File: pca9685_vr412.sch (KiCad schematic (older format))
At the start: 51 parts, among them J1 I2Cbus, J10 C4GND, J11 C4VDD, J12 C4VDD, J13 C4VDD, J14 C4VDD, J15 USB_B_Micro, J16 Conn_02x20, J2 Conn_01x02, J3 LED03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

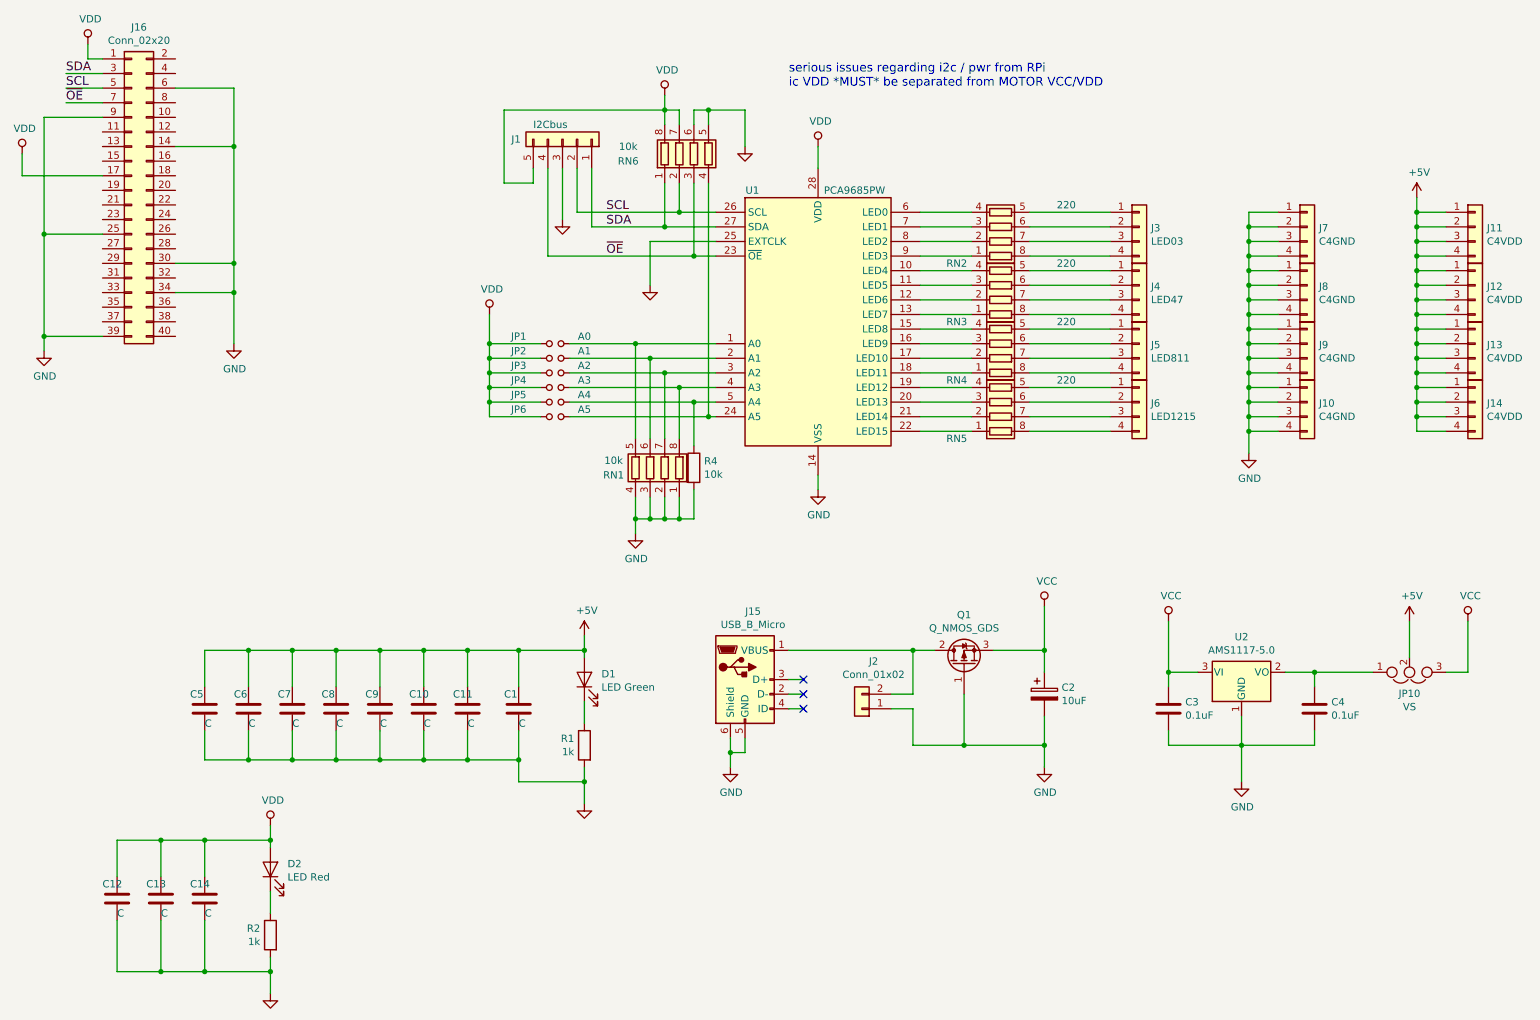
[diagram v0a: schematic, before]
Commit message: Updated layout
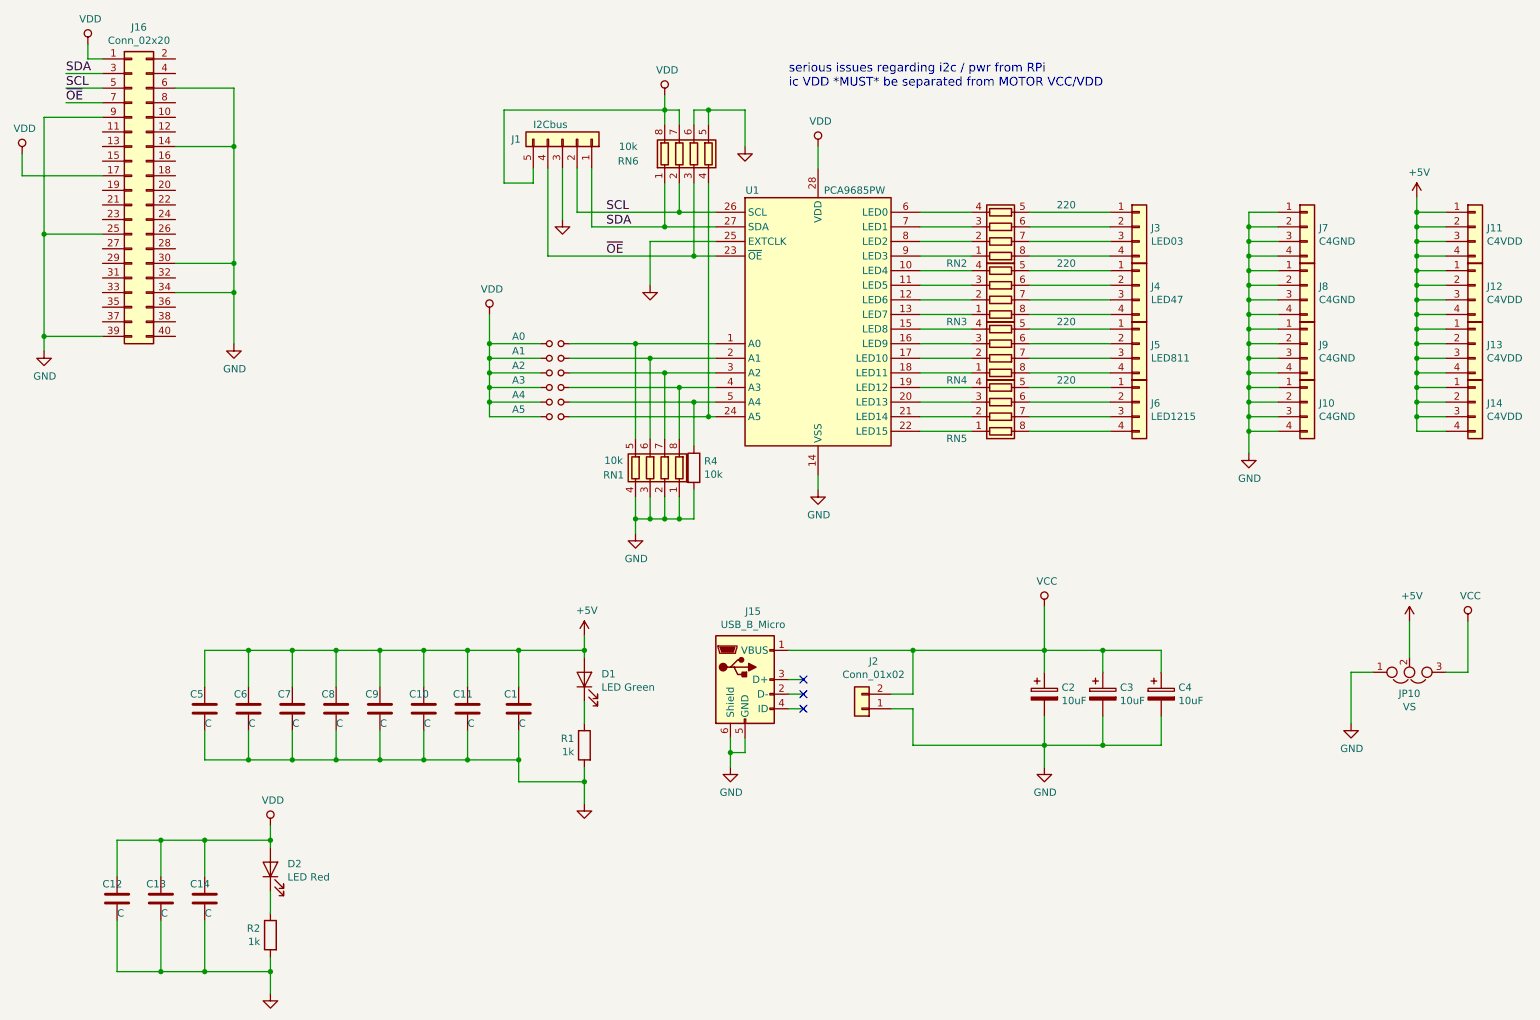
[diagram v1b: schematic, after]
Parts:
- removed C3, C4: 0.1uF, Capacitors_SMD:C_0603_HandSoldering, symbol C
- removed Q1: Q_NMOS_GDS, TO_SOT_Packages_SMD:SOT-23, symbol Q_PMOS_GDS
- removed U2: AMS1117-5.0, TO_SOT_Packages_SMD:SOT-223-3_TabPin2, symbol AMS1117-5.0
- added C3, C4: 10uF, Capacitors_SMD:CP_Elec_5x5.3, symbol CP
- renumbered JP1 to A0, JP2 to A1, JP3 to A2, JP4 to A3, JP5 to A4, JP6 to A5
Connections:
- net GND: now also JP10.1, C3.2, C4.2
- net VCC: now also J15.1 (VBUS), J2.2 (Pin_2), C3.1, C4.1
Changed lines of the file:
@@
 $EndComp
 $Comp
-L Jumper_NO_Small JP1
+L Jumper_NO_Small A0
 U 1 1 5D06A234
 P 4300 2950
-F 0 "JP1" H 4050 3000 50  0000 C CNN
-F 1 "A0" H 4500 3000 50  0000 C CNN
+F 0 "A0" H 4050 3000 50  0000 C CNN
+F 1 "A0" H 4500 3000 50  0001 C CNN
 F 2 "Jumper:SolderJumper_Triangular_0603" H 4300 2950 50  0001 C CNN
 F 3 "" H 4300 2950 50  0001 C CNN
@@
 $EndComp
 $Comp
-L Jumper_NO_Small JP2
+L Jumper_NO_Small A1
 U 1 1 5D06A4A7
 P 4300 3050
-F 0 "JP2" H 4050 3100 50  0000 C CNN
-F 1 "A1" H 4500 3100 50  0000 C CNN
+F 0 "A1" H 4050 3100 50  0000 C CNN
+F 1 "A1" H 4500 3100 50  0001 C CNN
 F 2 "Jumper:SolderJumper_Triangular_0603" H 4300 3050 50  0001 C CNN
 F 3 "" H 4300 3050 50  0001 C CNN
@@
 $EndComp
 $Comp
-L Jumper_NO_Small JP3
+L Jumper_NO_Small A2
 U 1 1 5D06A4FE
 P 4300 3150
-F 0 "JP3" H 4050 3200 50  0000 C CNN
-F 1 "A2" H 4500 3200 50  0000 C CNN
+F 0 "A2" H 4050 3200 50  0000 C CNN
+F 1 "A2" H 4500 3200 50  0001 C CNN
 F 2 "Jumper:SolderJumper_Triangular_0603" H 4300 3150 50  0001 C CNN
 F 3 "" H 4300 3150 50  0001 C CNN
@@
 $EndComp
 $Comp
-L Jumper_NO_Small JP4
+L Jumper_NO_Small A3
 U 1 1 5D06A550
 P 4300 3250
-F 0 "JP4" H 4050 3300 50  0000 C CNN
-F 1 "A3" H 4500 3300 50  0000 C CNN
+F 0 "A3" H 4050 3300 50  0000 C CNN
+F 1 "A3" H 4500 3300 50  0001 C CNN
 F 2 "Jumper:SolderJumper_Triangular_0603" H 4300 3250 50  0001 C CNN
 F 3 "" H 4300 3250 50  0001 C CNN
@@
 $EndComp
 $Comp
-L Jumper_NO_Small JP5
+L Jumper_NO_Small A4
 U 1 1 5D06A5BC
 P 4300 3350
-F 0 "JP5" H 4050 3400 50  0000 C CNN
-F 1 "A4" H 4500 3400 50  0000 C CNN
+F 0 "A4" H 4050 3400 50  0000 C CNN
+F 1 "A4" H 4500 3400 50  0001 C CNN
 F 2 "Jumper:SolderJumper_Triangular_0603" H 4300 3350 50  0001 C CNN
 F 3 "" H 4300 3350 50  0001 C CNN
@@
 $EndComp
 $Comp
-L Jumper_NO_Small JP6
+L Jumper_NO_Small A5
 U 1 1 5D06A614
 P 4300 3450
-F 0 "JP6" H 4050 3500 50  0000 C CNN
-F 1 "A5" H 4500 3500 50  0000 C CNN
+F 0 "A5" H 4050 3500 50  0000 C CNN
+F 1 "A5" H 4500 3500 50  0001 C CNN
 F 2 "Jumper:SolderJumper_Triangular_0603" H 4300 3450 50  0001 C CNN
 F 3 "" H 4300 3450 50  0001 C CNN
@@
 $EndComp
 $Comp
-L Q_PMOS_GDS Q1
-U 1 1 5D06E159
-P 7100 5150
-F 0 "Q1" V 7443 5150 50  0000 C CNN
-F 1 "Q_NMOS_GDS" V 7352 5150 50  0000 C CNN
-F 2 "TO_SOT_Packages_SMD:SOT-23" H 7300 5250 50  0001 C CNN
-F 3 "" H 7100 5150 50  0001 C CNN
-	1    7100 5150
-	0    -1   -1   0
-$EndComp
-$Comp
 L Conn_01x02 J2
 U 1 1 5D06E552
@@
 $EndComp
 $Comp
-L AMS1117-5.0 U2
-U 1 1 5D06F528
-P 9000 5200
-F 0 "U2" H 9000 5442 50  0000 C CNN
-F 1 "AMS1117-5.0" H 9000 5351 50  0000 C CNN
-F 2 "TO_SOT_Packages_SMD:SOT-223-3_TabPin2" H 9000 5400 50  0001 C CNN
-F 3 "" H 9100 4950 50  0001 C CNN
-	1    9000 5200
-	1    0    0    -1
-$EndComp
-$Comp
-L C C3
-U 1 1 5D06F63C
-P 8500 5450
-F 0 "C3" H 8615 5496 50  0000 L CNN
-F 1 "0.1uF" H 8615 5405 50  0000 L CNN
-F 2 "Capacitors_SMD:C_0603_HandSoldering" H 8538 5300 50  0001 C CNN
-F 3 "" H 8500 5450 50  0001 C CNN
-	1    8500 5450
-	1    0    0    -1
-$EndComp
-$Comp
-L C C4
-U 1 1 5D06F759
-P 9500 5450
-F 0 "C4" H 9615 5496 50  0000 L CNN
-F 1 "0.1uF" H 9615 5405 50  0000 L CNN
-F 2 "Capacitors_SMD:C_0603_HandSoldering" H 9538 5300 50  0001 C CNN
-F 3 "" H 9500 5450 50  0001 C CNN
-	1    9500 5450
-	1    0    0    -1
-$EndComp
-$Comp
 L GND #PWR014
 U 1 1 5D06FAF1
-P 9000 5950
-F 0 "#PWR014" H 9000 5700 50  0001 C CNN
-F 1 "GND" H 9005 5777 50  0000 C CNN
-F 2 "" H 9000 5950 50  0001 C CNN
-F 3 "" H 9000 5950 50  0001 C CNN
-	1    9000 5950
-	1    0    0    -1
-$EndComp
-$Comp
-L VCC #PWR015
-U 1 1 5D06FFCB
-P 8500 4850
-F 0 "#PWR015" H 8500 4700 50  0001 C CNN
-F 1 "VCC" H 8517 5023 50  0000 C CNN
-F 2 "" H 8500 4850 50  0001 C CNN
-F 3 "" H 8500 4850 50  0001 C CNN
-	1    8500 4850
-	1    0    0    -1
-$EndComp
-$Comp
-L +5V #PWR016
+P 9750 5550
+F 0 "#PWR014" H 9750 5300 50  0001 C CNN
+F 1 "GND" H 9755 5377 50  0000 C CNN
+F 2 "" H 9750 5550 50  0001 C CNN
+F 3 "" H 9750 5550 50  0001 C CNN
+	1    9750 5550
+	1    0    0    -1
+$EndComp
+$Comp
+L +5V #PWR015
 U 1 1 5D07075D
 P 10150 4850
-F 0 "#PWR016" H 10150 4700 50  0001 C CNN
+F 0 "#PWR015" H 10150 4700 50  0001 C CNN
 F 1 "+5V" H 10167 5023 50  0000 C CNN
 F 2 "" H 10150 4850 50  0001 C CNN
@@
 $EndComp
 $Comp
-L +5V #PWR017
+L +5V #PWR016
 U 1 1 5D069767
 P 10200 1950
-F 0 "#PWR017" H 10200 1800 50  0001 C CNN
+F 0 "#PWR016" H 10200 1800 50  0001 C CNN
 F 1 "+5V" H 10217 2123 50  0000 C CNN
 F 2 "" H 10200 1950 50  0001 C CNN
@@
 $EndComp
 $Comp
-L VCC #PWR018
+L VCC #PWR017
 U 1 1 5D0E12C9
 P 10550 4850
-F 0 "#PWR018" H 10550 4700 50  0001 C CNN
+F 0 "#PWR017" H 10550 4700 50  0001 C CNN
 F 1 "VCC" H 10567 5023 50  0000 C CNN
 F 2 "" H 10550 4850 50  0001 C CNN
@@
 	6750 5350 6750 5050
 Wire Wire Line
-	5900 5050 6900 5050
+	5900 5050 8450 5050
 Wire Wire Line
 	6600 5450 6750 5450
@@
 	6750 5450 6750 5700
 Wire Wire Line
-	6750 5700 7650 5700
-Wire Wire Line
-	7300 5050 7650 5050
+	6750 5700 8450 5700
 Wire Wire Line
 	7650 4750 7650 5200
@@
 Wire Wire Line
 	7650 5500 7650 5850
-Wire Wire Line
-	7100 5350 7100 5700
-Connection ~ 7100 5700
 Connection ~ 7650 5700
 Wire Wire Line
-	8500 4850 8500 5300
-Wire Wire Line
-	8500 5200 8700 5200
-Wire Wire Line
-	9300 5200 9900 5200
-Wire Wire Line
-	9500 5200 9500 5300
-Wire Wire Line
-	8500 5600 8500 5700
-Wire Wire Line
-	8500 5700 9500 5700
-Wire Wire Line
-	9000 5500 9000 5950
-Connection ~ 9000 5700
-Wire Wire Line
-	9500 5700 9500 5600
-Connection ~ 8500 5200
-Connection ~ 9500 5200
+	9750 5200 9900 5200
+Wire Wire Line
+	9750 5200 9750 5550
 Wire Wire Line
 	1900 5050 4500 5050
@@
 $EndComp
 $Comp
-L GND #PWR019
+L GND #PWR018
 U 1 1 5D8F8C6E
 P 5500 5850
-F 0 "#PWR019" H 5500 5600 50  0001 C CNN
+F 0 "#PWR018" H 5500 5600 50  0001 C CNN
 F 1 "GND" H 5505 5677 50  0000 C CNN
 F 2 "" H 5500 5850 50  0001 C CNN
@@
 $EndComp
 $Comp
-L GND #PWR020
+L GND #PWR019
 U 1 1 5D930AA3
 P 2350 7400
-F 0 "#PWR020" H 2350 7150 50  0001 C CNN
+F 0 "#PWR019" H 2350 7150 50  0001 C CNN
 F 1 "GND" H 2355 7227 50  0001 C CNN
 F 2 "" H 2350 7400 50  0001 C CNN
@@
 	1300 6350 2350 6350
 $Comp
-L VDD #PWR021
+L VDD #PWR020
 U 1 1 5D932621
 P 2350 6250
-F 0 "#PWR021" H 2350 6100 50  0001 C CNN
+F 0 "#PWR020" H 2350 6100 50  0001 C CNN
 F 1 "VDD" H 2367 6423 50  0000 C CNN
 F 2 "" H 2350 6250 50  0001 C CNN
@@
 ~OE~
 $Comp
-L VDD #PWR022
+L VDD #PWR021
 U 1 1 5D9B90EA
 P 1100 900
-F 0 "#PWR022" H 1100 750 50  0001 C CNN
+F 0 "#PWR021" H 1100 750 50  0001 C CNN
 F 1 "VDD" H 1117 1073 50  0000 C CNN
 F 2 "" H 1100 900 50  0001 C CNN
@@
 Connection ~ 800  2900
 $Comp
-L GND #PWR023
+L GND #PWR022
 U 1 1 5D9BA12C
 P 800 3000
-F 0 "#PWR023" H 800 2750 50  0001 C CNN
+F 0 "#PWR022" H 800 2750 50  0001 C CNN
 F 1 "GND" H 805 2827 50  0000 C CNN
 F 2 "" H 800 3000 50  0001 C CNN
@@
 $EndComp
 $Comp
-L GND #PWR024
+L GND #PWR023
 U 1 1 5D9BA236
 P 2100 2950
-F 0 "#PWR024" H 2100 2700 50  0001 C CNN
+F 0 "#PWR023" H 2100 2700 50  0001 C CNN
 F 1 "GND" H 2105 2777 50  0000 C CNN
 F 2 "" H 2100 2950 50  0001 C CNN
@@
 	650  1800 650  1650
 $Comp
-L VDD #PWR025
+L VDD #PWR024
 U 1 1 5D9BA566
 P 650 1650
-F 0 "#PWR025" H 650 1500 50  0001 C CNN
+F 0 "#PWR024" H 650 1500 50  0001 C CNN
 F 1 "VDD" H 667 1823 50  0000 C CNN
 F 2 "" H 650 1650 50  0001 C CNN
@@
 Text Label 950  1300 0    60   ~ 0
 ~OE~
+$Comp
+L CP C3
+U 1 1 5ECA5F15
+P 8050 5350
+F 0 "C3" H 8168 5396 50  0000 L CNN
+F 1 "10uF" H 8168 5305 50  0000 L CNN
+F 2 "Capacitors_SMD:CP_Elec_5x5.3" H 8088 5200 50  0001 C CNN
+F 3 "" H 8050 5350 50  0001 C CNN
+	1    8050 5350
+	1    0    0    -1
+$EndComp
+$Comp
+L CP C4
+U 1 1 5ECA5FC7
+P 8450 5350
+F 0 "C4" H 8568 5396 50  0000 L CNN
+F 1 "10uF" H 8568 5305 50  0000 L CNN
+F 2 "Capacitors_SMD:CP_Elec_5x5.3" H 8488 5200 50  0001 C CNN
+F 3 "" H 8450 5350 50  0001 C CNN
+	1    8450 5350
+	1    0    0    -1
+$EndComp
+Wire Wire Line
+	8050 5050 8050 5200
+Wire Wire Line
+	8050 5700 8050 5500
+Wire Wire Line
+	8450 5050 8450 5200
+Connection ~ 8050 5050
+Wire Wire Line
+	8450 5700 8450 5500
+Connection ~ 8050 5700
 $EndSCHEMATC
